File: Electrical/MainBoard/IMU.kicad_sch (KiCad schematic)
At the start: 1 part, among them J26 Conn_02x04_Odd_Even

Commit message: Update some parts
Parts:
- J26: Mfr (none) -> METZ CONNECT USA Inc.; Mfr P/N (none) -> PR20204VBDN; Supplier 1 P/N 10129381-908001BLF-ND -> 1849-PR20204VBDN-ND
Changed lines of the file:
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@@
 			)
 		)
-		(property "Description" ""
+		(property "Description" "CONN HEADER VERT 8POS 2.54MM"
 			(at 187.325 142.24 0)
 			(effects
@@
 			)
 		)
-		(property "Mfr" ""
+		(property "Mfr" "METZ CONNECT USA Inc."
 			(at 187.325 142.24 0)
 			(effects
@@
 			)
 		)
-		(property "Mfr P/N" ""
+		(property "Mfr P/N" "PR20204VBDN"
 			(at 187.325 142.24 0)
 			(effects
@@
 			)
 		)
-		(property "Supplier 1 P/N" "10129381-908001BLF-ND"
+		(property "Supplier 1 P/N" "1849-PR20204VBDN-ND"
 			(at 187.325 142.24 0)
 			(effects

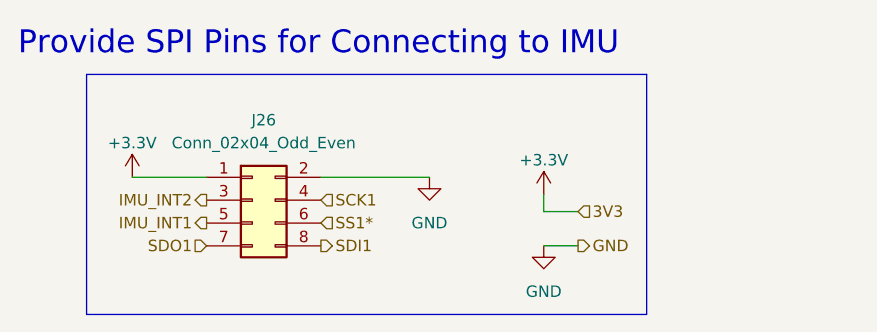
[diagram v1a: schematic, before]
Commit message: Change some connections to picoblade, add env sensor connector
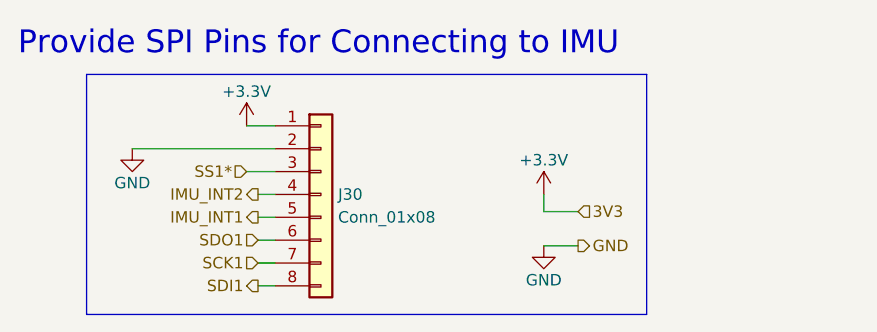
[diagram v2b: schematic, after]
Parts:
- removed J26: Conn_02x04_Odd_Even, Connector_PinHeader_2.54mm:PinHeader_2x04_P2.54mm_Vertical, symbol Connector_Generic:Conn_02x04_Odd_Even
- added J30: Conn_01x08, Connector_Molex:Molex_PicoBlade_53047-0810_1x08_P1.25mm_Vertical, symbol Connector_Generic:Conn_01x08
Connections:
- net +3.3V: now also J30.1 (Pin_1)
- net GND: now also J30.2 (Pin_2)
- net IMU_INT1: now also J30.5 (Pin_5)
- net IMU_INT2: now also J30.4 (Pin_4)
- net SCK1: now also J30.7 (Pin_7)
- net SDI1: now also J30.8 (Pin_8)
- net SDO1: now also J30.6 (Pin_6)
- net SS1*: now also J30.3 (Pin_3)

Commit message: Use more molex picoblades and make schematic prettier
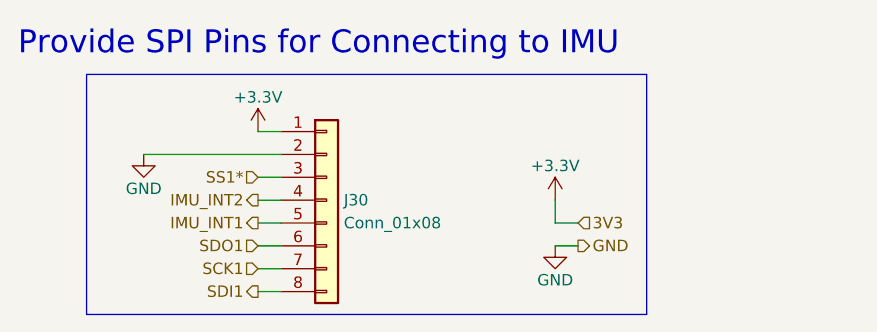
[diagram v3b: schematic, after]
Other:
- moved on the sheet: J30
